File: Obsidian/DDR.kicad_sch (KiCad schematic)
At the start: 59 parts, among them U2 MT41K512M16HA-125_E / MT41K51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

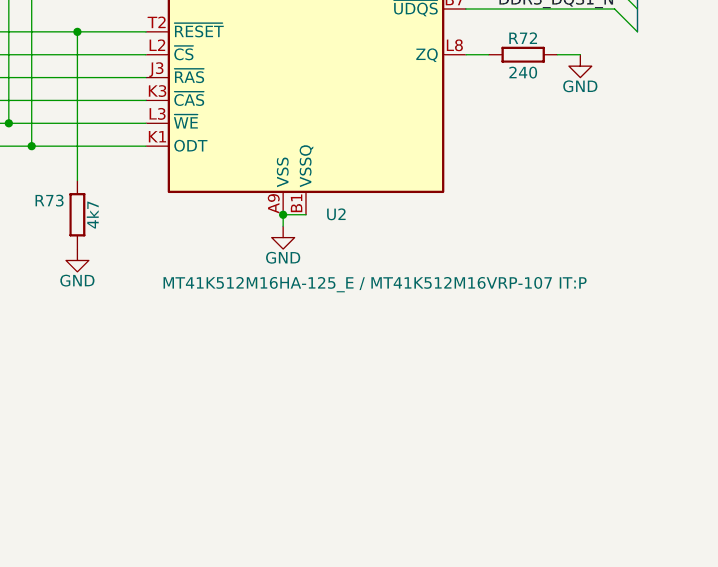
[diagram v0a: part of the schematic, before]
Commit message: Update the schematic, PCB
- Cleaning silkcreen
- Solving uncoupled length issues
- Solving unfound footprint issues
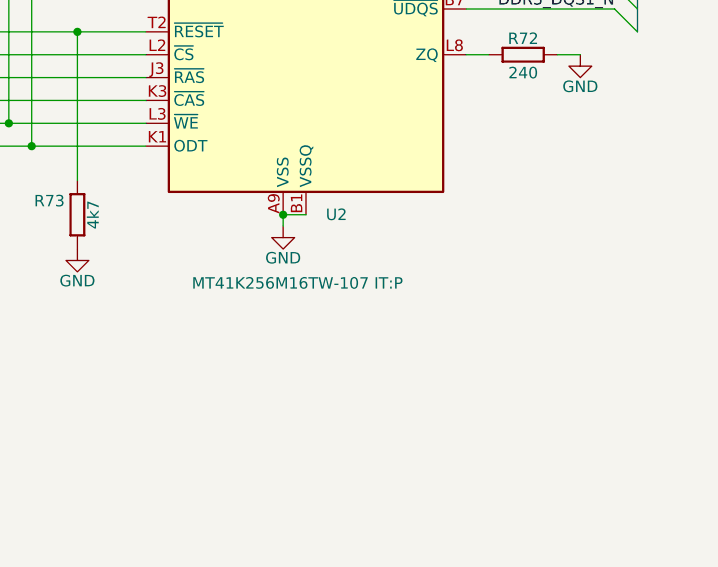
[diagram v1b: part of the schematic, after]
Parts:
- U2: value MT41K512M16HA-125_E / MT41K512M16VRP-107 IT:P -> MT41K256M16TW-107 IT:P; LCSC C2831669 -> C367428
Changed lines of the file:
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@@
 			)
 		)
-		(property "Value" "MT41K512M16HA-125_E / MT41K512M16VRP-107 IT:P"
-			(at 149.098 146.05 0)
+		(property "Value" "MT41K256M16TW-107 IT:P"
+			(at 152.4 146.05 0)
 			(effects
 				(font
@@
 			)
 		)
-		(property "Datasheet" "${KIPRJMOD}/datasheet/C2831669.pdf"
+		(property "Datasheet" "${KIPRJMOD}/datasheet/C367428.pdf"
 			(at 163.83 26.67 0)
 			(effects
@@
 			)
 		)
-		(property "LCSC" "C2831669"
+		(property "LCSC" "C367428"
 			(at 165.1 95.25 0)
 			(effects

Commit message: Update schematic for out of stock components
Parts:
- R168: value R0402_80R6_1%_0.1W_100PPM -> R0402_80R6_1%_0.0625W_100PPM; LCSC C2077034 -> C185392
- R73: LCSC C25900 -> C2906869
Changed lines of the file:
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@@
 			)
 		)
-		(property "Datasheet" "${KIPRJMOD}/datasheet/C25900.pdf"
+		(property "Datasheet" "${KIPRJMOD}/datasheet/C2906869.pdf"
 			(at 148.463 142.24 0)
 			(effects
@@
 			)
 		)
-		(property "LCSC" "C25900"
+		(property "LCSC" "C2906869"
 			(at 139.7 142.24 90)
 			(effects
@@
 			)
 		)
-		(property "Value" "R0402_80R6_1%_0.1W_100PPM"
+		(property "Value" "R0402_80R6_1%_0.0625W_100PPM"
 			(at 105.41 114.173 0)
 			(effects
@@
 			)
 		)
-		(property "Datasheet" "${KIPRJMOD}/datasheet/C2077034.pdf"
+		(property "Datasheet" "${KIPRJMOD}/datasheet/C185392.pdf"
 			(at 105.41 117.983 0)
 			(effects
@@
 			)
 		)
-		(property "LCSC" "C2077034"
+		(property "LCSC" "C185392"
 			(at 105.41 109.22 0)
 			(effects
